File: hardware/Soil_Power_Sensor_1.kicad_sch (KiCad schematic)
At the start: 23 parts, among them J1 Screw_Terminal_01x05, U1 MAX9944, U2 INA296A, U4 THS4532, U6 ADS1219

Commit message: Updated BOM
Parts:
- JP1, JP2, JP3: now left out of the parts list
- RSENSE1: now not fitted; now left out of the parts list
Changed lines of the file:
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@@
 		(unit 1)
 		(exclude_from_sim no)
-		(in_bom yes)
+		(in_bom no)
 		(on_board yes)
 		(dnp no)
@@
 		(unit 1)
 		(exclude_from_sim no)
-		(in_bom yes)
+		(in_bom no)
 		(on_board yes)
 		(dnp no)
@@
 		(unit 1)
 		(exclude_from_sim no)
-		(in_bom yes)
+		(in_bom no)
 		(on_board yes)
 		(dnp no)
@@
 		(unit 1)
 		(exclude_from_sim no)
-		(in_bom yes)
+		(in_bom no)
 		(on_board yes)
-		(dnp no)
+		(dnp yes)
 		(property "Reference" "RSENSE1"
 			(at 33.02 134.62 0)

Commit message: Updated BOM for JLCPCB
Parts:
- U2: LCSC (none) -> C7577680
- U4: LCSC (none) -> C2059559

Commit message: Updated BOM with necessary JCLPCB part numbers
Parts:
- R1, R2, R6, R7: LCSC (none) -> C122538
- R3, R5: LCSC (none) -> C95204
- R4: LCSC (none) -> C858646
- R8, R9: LCSC (none) -> C515607
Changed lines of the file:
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@@
 			)
 		)
-		(property "LCSC" ""
+		(property "LCSC" "C95204"
 			(at 114.3 113.03 0)
 			(effects
@@
 			)
 		)
-		(property "LCSC" ""
+		(property "LCSC" "C122538"
 			(at 134.62 22.86 0)
 			(effects
@@
 			)
 		)
-		(property "LCSC" ""
+		(property "LCSC" "C122538"
 			(at 134.62 73.66 0)
 			(effects
@@
 			)
 		)
-		(property "LCSC" ""
+		(property "LCSC" "C95204"
 			(at 114.3 154.94 0)
 			(effects
@@
 			)
 		)
-		(property "LCSC" ""
+		(property "LCSC" "C858646"
 			(at 35.56 115.57 0)
 			(effects
@@
 			)
 		)
-		(property "LCSC" ""
+		(property "LCSC" "C122538"
 			(at 114.3 22.86 0)
 			(effects
@@
 			)
 		)
-		(property "LCSC" ""
+		(property "LCSC" "C122538"
 			(at 114.3 73.66 0)
 			(effects
@@
 			)
 		)
-		(property "LCSC" ""
+		(property "LCSC" "C515607"
 			(at 132.08 113.03 0)
 			(effects
@@
 			)
 		)
-		(property "LCSC" ""
+		(property "LCSC" "C515607"
 			(at 132.08 154.94 0)
 			(effects

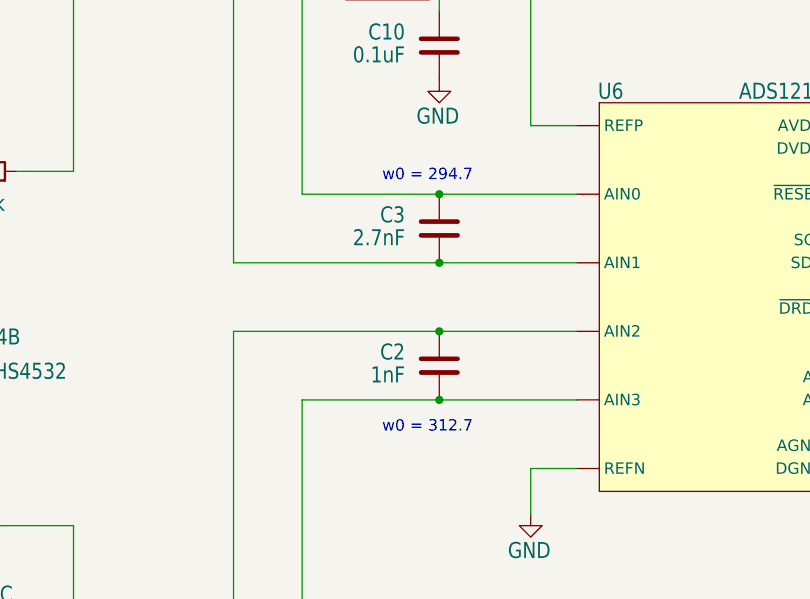
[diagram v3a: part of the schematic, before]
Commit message: Removed C2, C3
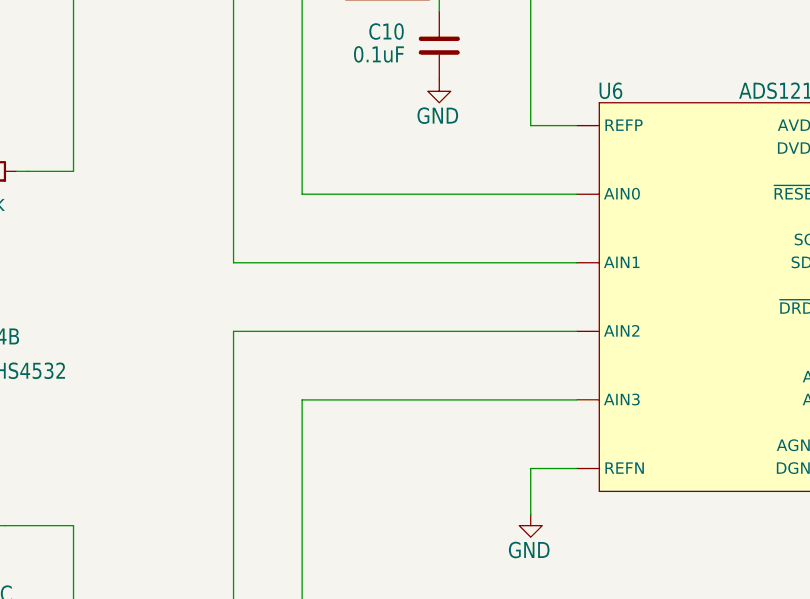
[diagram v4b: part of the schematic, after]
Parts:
- removed C2: 1nF, Capacitor_SMD:C_0603_1608Metric, symbol Device:C
- removed C3: 2.7nF, Capacitor_SMD:C_0603_1608Metric, symbol Device:C
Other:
- note removed: "w0 = 294.7"
- note removed: "w0 = 312.7"
